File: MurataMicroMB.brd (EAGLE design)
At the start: 90 x 63 mm, 47 parts, among them CON1 C-2395.MurataMicroSD, CON3 CON_MIL_10_ARM, CON4 C-2395.microSD, IC1 74LVC1G00DBV, IC2 IC_DCDC_LM27313, IC3 IC_LPC11U3XQFN33, IC4 IC_LDO_XX1117_4, Q1 CLOCK_CRYSTAL_4_3225, SW1 SW_TACTSW_2PP8073, SW2 SW_TACTSW_2PP8073, SW3 SW_TACTSW_2PP8073, X1 TSW-102-02-S-S

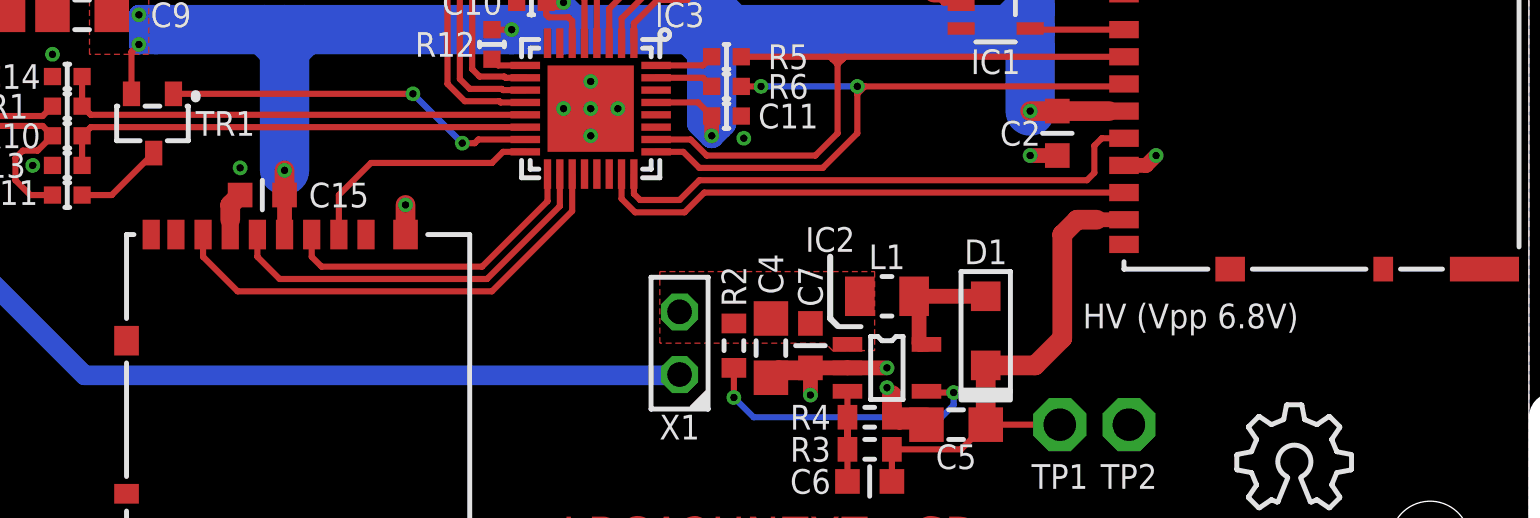
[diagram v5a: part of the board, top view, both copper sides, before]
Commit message: [ MB ] RCL value and size
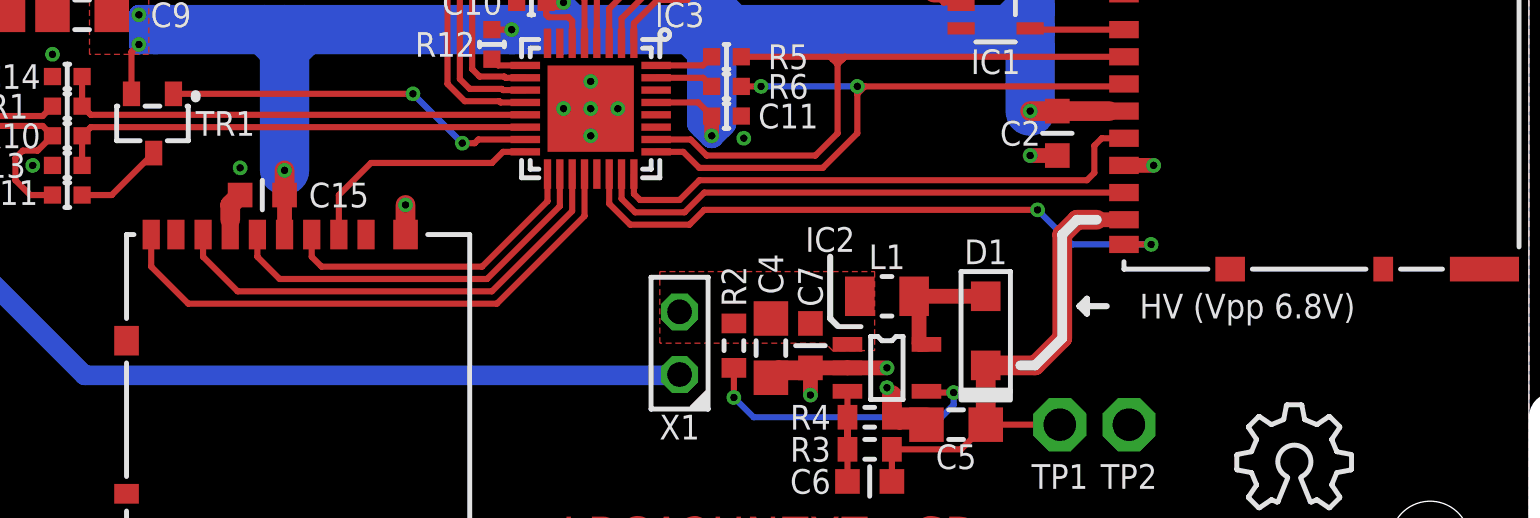
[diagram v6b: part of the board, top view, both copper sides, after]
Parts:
- C12, C3: value 18p -> 18p/1005
- C8, C9: value 4.7u -> 4.7u/1608
- R12, R7, R8, R9: value 10k -> 10k/1005
- R5, R6: value 100 -> 100/1005
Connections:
- new net DETECT1: CON1.SW_B, IC3.22
- new net DETECT2: CON4.SW_B, IC3.20
- net GND: now also CON1.SW_A, CON4.SW_A
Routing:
- net DETECT1: track 0.00 -> 25.4 mm, vias 0 -> 2
- net DETECT2: track 0.00 -> 22.6 mm
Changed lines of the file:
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@@
 <plain>
 <rectangle x1="53.6" y1="23.1" x2="54.4" y2="24.7" layer="41"/>
-<text x="66.3" y="23.1" size="1" layer="21" ratio="20" align="center">HV (Vpp 6.8V)</text>
+<text x="68.6" y="23.5" size="1" layer="21" ratio="20" align="center">HV (Vpp 6.8V)</text>
 <wire x1="59" y1="21.7" x2="59.7" y2="21.7" width="0.25" layer="41"/>
 <wire x1="59.7" y1="21.7" x2="60.5" y2="22.5" width="0.25" layer="41"/>
@@
 <wire x1="90.5" y1="53" x2="92.8" y2="53" width="0.25" layer="102"/>
 <text x="37.4" y="1.5" size="1.778" layer="21" ratio="17">board thickness t = 1.2mm</text>
+<wire x1="62.5" y1="27" x2="61.7" y2="27" width="0.4" layer="21"/>
+<wire x1="61.7" y1="27" x2="61.1" y2="26.4" width="0.4" layer="21"/>
+<wire x1="61.1" y1="26.4" x2="61.1" y2="22.2" width="0.4" layer="21"/>
+<wire x1="61.1" y1="22.2" x2="60" y2="21.1" width="0.4" layer="21"/>
+<wire x1="60" y1="21.1" x2="59.4" y2="21.1" width="0.4" layer="21"/>
+<wire x1="61.8" y1="23.5" x2="62.1" y2="23.8" width="0.25" layer="21"/>
+<wire x1="62.1" y1="23.8" x2="62.1" y2="23.2" width="0.25" layer="21"/>
+<wire x1="62.1" y1="23.2" x2="61.8" y2="23.5" width="0.25" layer="21"/>
+<wire x1="61.8" y1="23.5" x2="62.9" y2="23.5" width="0.25" layer="21"/>
 </plain>
 <attributes>
@@
 <attribute name="VALUE" x="37.4" y="34" size="1.27" layer="27" ratio="16" rot="R270"/>
 </element>
-<element name="C8" library="mylib" package="CR_2125" value="4.7u" x="17.2" y="35.3" smashed="yes">
+<element name="C8" library="mylib" package="CR_2125" value="4.7u/1608" x="17.2" y="35.3" smashed="yes">
 <attribute name="NAME" x="17.2" y="34" size="1" layer="25" ratio="20" align="center"/>
 <attribute name="VALUE" x="17.2" y="33.4" size="1" layer="27" ratio="20"/>
 </element>
-<element name="C9" library="mylib" package="CR_2125" value="4.7u" x="21.4" y="35.3" smashed="yes" rot="R180">
+<element name="C9" library="mylib" package="CR_2125" value="4.7u/1608" x="21.4" y="35.3" smashed="yes" rot="R180">
 <attribute name="NAME" x="25" y="35.3" size="1" layer="25" ratio="20" align="center"/>
 <attribute name="VALUE" x="21.4" y="37.2" size="1" layer="27" ratio="20" rot="R180"/>
@@
 <attribute name="VALUE" x="46.9" y="29.3" size="1" layer="27" font="vector" ratio="20"/>
 </element>
-<element name="R5" library="mylib" package="C0402" value="100" x="47.5" y="33.6" smashed="yes">
+<element name="R5" library="mylib" package="C0402" value="100/1005" x="47.5" y="33.6" smashed="yes">
 <attribute name="NAME" x="50" y="33.6" size="1" layer="25" font="vector" ratio="20" align="center"/>
 <attribute name="VALUE" x="46.9" y="31.7" size="1" layer="27" font="vector" ratio="20"/>
 </element>
-<element name="R6" library="mylib" package="C0402" value="100" x="47.5" y="32.4" smashed="yes">
+<element name="R6" library="mylib" package="C0402" value="100/1005" x="47.5" y="32.4" smashed="yes">
 <attribute name="NAME" x="50" y="32.4" size="1" layer="25" font="vector" ratio="20" align="center"/>
 <attribute name="VALUE" x="46.9" y="30.5" size="1" layer="27" font="vector" ratio="20"/>
 </element>
-<element name="R7" library="mylib" package="C0402" value="10k" x="46.9" y="38.9" smashed="yes" rot="R270">
+<element name="R7" library="mylib" package="C0402" value="10k/1005" x="46.9" y="38.9" smashed="yes" rot="R270">
 <attribute name="NAME" x="46.9" y="42" size="1" layer="25" font="vector" ratio="20" rot="R270" align="center"/>
 <attribute name="VALUE" x="45" y="39.5" size="1" layer="27" font="vector" ratio="20" rot="R270"/>
 </element>
-<element name="R8" library="mylib" package="C0402" value="10k" x="48.3" y="38.9" smashed="yes" rot="R270">
+<element name="R8" library="mylib" package="C0402" value="10k/1005" x="48.3" y="38.9" smashed="yes" rot="R270">
 <attribute name="NAME" x="48.3" y="42" size="1" layer="25" font="vector" ratio="20" rot="R270" align="center"/>
 <attribute name="VALUE" x="46.4" y="39.5" size="1" layer="27" font="vector" ratio="20" rot="R270"/>
 </element>
-<element name="R9" library="mylib" package="C0402" value="10k" x="45.5" y="38.9" smashed="yes" rot="R270">
+<element name="R9" library="mylib" package="C0402" value="10k/1005" x="45.5" y="38.9" smashed="yes" rot="R270">
 <attribute name="NAME" x="45.5" y="42" size="1" layer="25" font="vector" ratio="20" rot="R270" align="center"/>
 <attribute name="VALUE" x="43.6" y="39.5" size="1" layer="27" font="vector" ratio="20" rot="R270"/>
@@
 <attribute name="NAME" x="39.4" y="39.5" size="1" layer="25" font="vector" ratio="20" rot="R180" align="center"/>
 </element>
-<element name="C3" library="mylib" package="C0402" value="18p" x="41.9" y="42.3" smashed="yes">
+<element name="C3" library="mylib" package="C0402" value="18p/1005" x="41.9" y="42.3" smashed="yes">
 <attribute name="NAME" x="39.8" y="42.3" size="1" layer="25" font="vector" ratio="20" rot="R180" align="center"/>
 <attribute name="VALUE" x="41.3" y="40.4" size="1" layer="27" font="vector" ratio="20"/>
 </element>
-<element name="C12" library="mylib" package="C0402" value="18p" x="44.3" y="38.9" smashed="yes" rot="R90">
+<element name="C12" library="mylib" package="C0402" value="18p/1005" x="44.3" y="38.9" smashed="yes" rot="R90">
 <attribute name="NAME" x="44.3" y="42.1" size="1" layer="25" font="vector" ratio="20" rot="R90" align="center"/>
 <attribute name="VALUE" x="46.2" y="38.3" size="1" layer="27" font="vector" ratio="20" rot="R90"/>
@@
 <attribute name="VALUE" x="21.4" y="29.9" size="1" layer="27" font="vector" ratio="20" rot="R180"/>
 </element>
-<element name="R12" library="mylib" package="C0402" value="10k" x="38" y="34.1" smashed="yes" rot="R270">
+<element name="R12" library="mylib" package="C0402" value="10k/1005" x="38" y="34.1" smashed="yes" rot="R270">
 <attribute name="NAME" x="36.1" y="34.1" size="1" layer="25" font="vector" ratio="20" align="center"/>
 <attribute name="VALUE" x="36.1" y="34.7" size="1" layer="27" font="vector" ratio="20" rot="R270"/>
@@
 <contactref element="C2" pad="2"/>
 <via x="59.8" y="29.6" extent="1-16" drill="0.3"/>
-<via x="64.9" y="29.6" extent="1-16" drill="0.3"/>
+<via x="64.8" y="29.2" extent="1-16" drill="0.3"/>
 <contactref element="CON1" pad="SHLD@4"/>
 <contactref element="CON1" pad="SHLD"/>
@@
 <wire x1="50.9" y1="19.9" x2="50.9" y2="21" width="0.6" layer="1"/>
 <wire x1="59.8" y1="29.6" x2="60.9" y2="29.6" width="0.6" layer="1"/>
-<wire x1="64.9" y1="29.6" x2="64.5" y2="29.2" width="0.6" layer="1"/>
-<wire x1="64.5" y1="29.2" x2="63.6" y2="29.2" width="0.6" layer="1"/>
+<wire x1="64.8" y1="29.2" x2="63.6" y2="29.2" width="0.6" layer="1"/>
 <contactref element="TP2" pad="TP"/>
 <contactref element="C8" pad="2"/>
@@
 <wire x1="41" y1="38.3" x2="41.1" y2="38.3" width="0.6" layer="1"/>
 <wire x1="34.5" y1="27.6" x2="34.5" y2="26.4" width="0.8" layer="1"/>
+<contactref element="CON4" pad="SW_A"/>
+<contactref element="CON1" pad="SW_A"/>
 </signal>
 <signal name="D-">
@@
 <wire x1="31.8" y1="28" x2="31.8" y2="26.4" width="0.25" layer="1"/>
 </signal>
+<signal name="DETECT2">
+<contactref element="IC3" pad="20"/>
+<contactref element="CON4" pad="SW_B"/>
+<wire x1="24.2" y1="26.4" x2="24.2" y2="25.1" width="0.25" layer="1"/>
+<wire x1="24.2" y1="25.1" x2="25.7" y2="23.6" width="0.25" layer="1"/>
+<wire x1="25.7" y1="23.6" x2="38.2" y2="23.6" width="0.25" layer="1"/>
+<wire x1="38.2" y1="23.6" x2="41.75" y2="27.15" width="0.25" layer="1"/>
+<wire x1="41.75" y1="28.85" x2="41.75" y2="27.15" width="0.25" layer="1"/>
+</signal>
+<signal name="DETECT1">
+<contactref element="IC3" pad="22"/>
+<contactref element="CON1" pad="SW_B"/>
+<wire x1="63.6" y1="26" x2="64.7" y2="26" width="0.25" layer="1"/>
+<via x="64.7" y="26" extent="1-16" drill="0.3"/>
+<wire x1="64.7" y1="26" x2="61.5" y2="26" width="0.25" layer="16"/>
+<wire x1="61.5" y1="26" x2="60.1" y2="27.4" width="0.25" layer="16"/>
+<via x="60.1" y="27.4" extent="1-16" drill="0.3"/>
+<wire x1="60.1" y1="27.4" x2="46.6" y2="27.4" width="0.25" layer="1"/>
+<wire x1="46.6" y1="27.4" x2="46" y2="26.8" width="0.25" layer="1"/>
+<wire x1="46" y1="26.8" x2="43.6" y2="26.8" width="0.25" layer="1"/>
+<wire x1="43.6" y1="26.8" x2="42.75" y2="27.65" width="0.25" layer="1"/>
+<wire x1="42.75" y1="28.85" x2="42.75" y2="27.65" width="0.25" layer="1"/>
+</signal>
 </signals>

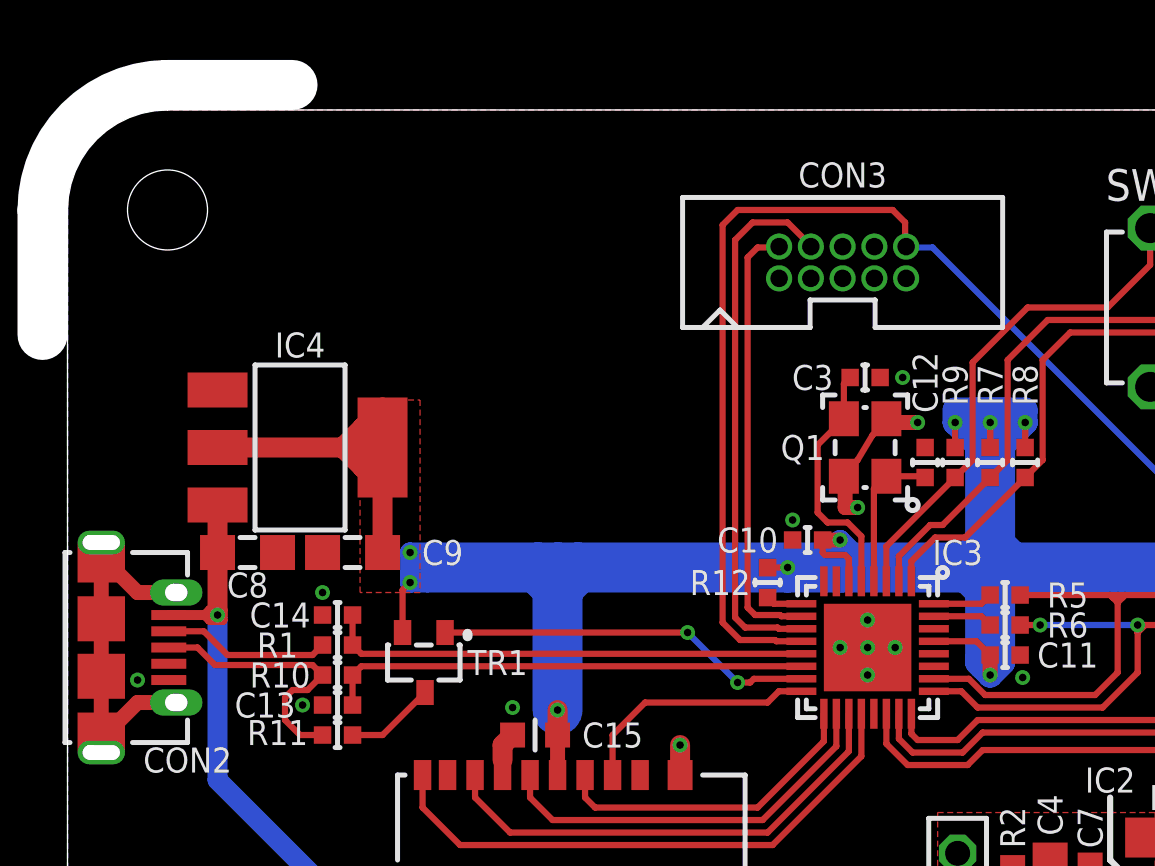
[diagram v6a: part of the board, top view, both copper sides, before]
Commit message: [ MB ] add LED1/R13/R14
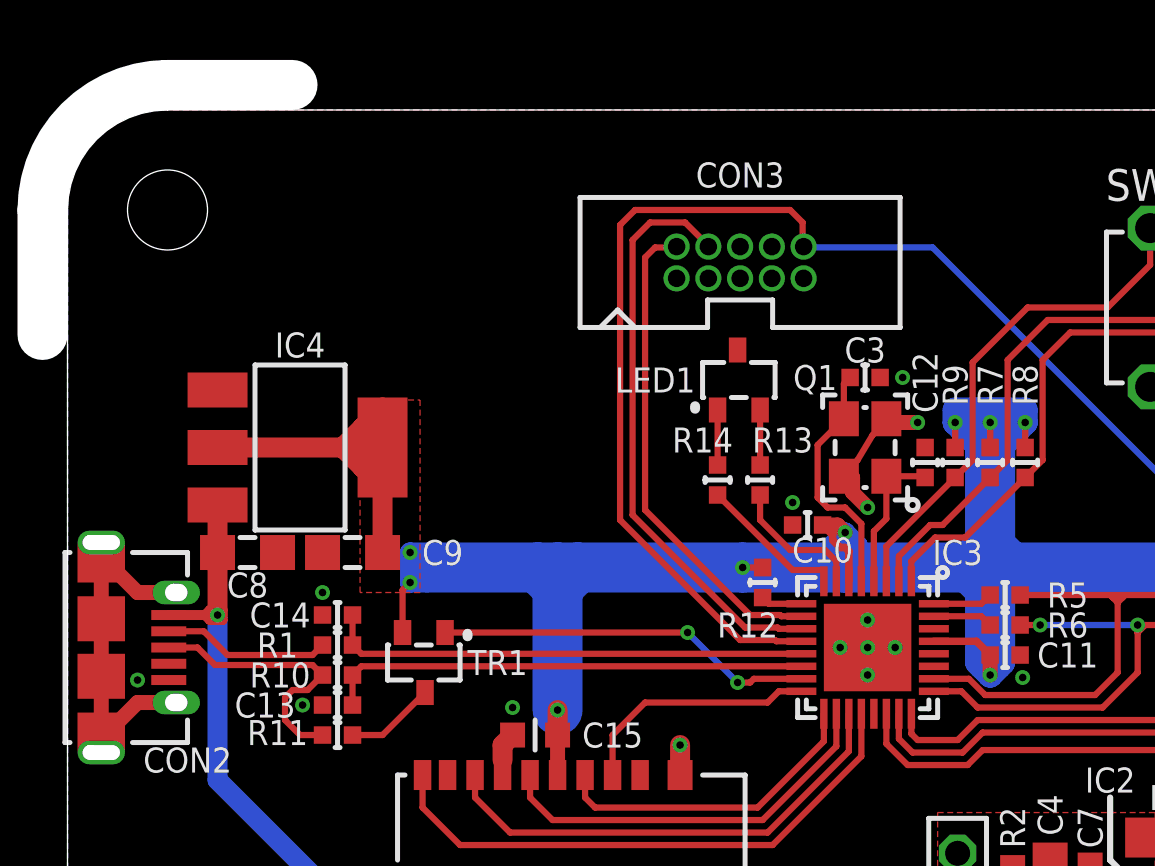
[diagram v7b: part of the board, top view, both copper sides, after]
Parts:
- added LED1: (no value), mylib:SOT95P300X140-3N
- added R13, R14: 100/1005, mylib:C0402
- IC2: value IC_DCDC_LM27313 -> 296-35164-1-ND
- moved CON3 4.10 mm to (36.9, 46.9)
- moved C10 0.60 mm to (39.6, 36.4)
- moved R12 0.20 mm to (37.8, 34.1)
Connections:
- new net N$1: IC3.8, R14.1
- new net N$14: IC3.7, R13.1
- new net N$15: LED1.2, R13.2
- new net N$16: LED1.1, R14.2
- net GND: now also LED1.3
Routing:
- net N$1: track 0.00 -> 5.94 mm
- net NSRST: track 48.7 -> 54.5 mm
- net N$14: track 0.00 -> 5.53 mm
- net N$16: track 0.00 -> 2.20 mm
- net N$15: track 0.00 -> 2.20 mm
- net SWDIO: track 17.7 -> 19.6 mm
- net SWCLK: track 21.7 -> 23.4 mm
- net 3.3V: track 134.7 -> 135.6 mm

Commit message: [ MB ][ SCH ] values and details change
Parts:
- C1, C10, C11: value 0.1u -> 0.1u/1005
- C15, C2, C7: value 0.1u -> 0.1u/1608
- C4, C5: value 4.7u -> 4.7u/2012
- C6: value NM -> NM/1608
- C8, C9: value 4.7u/1608 -> 4.7u/2012
- CON1: value C-2395.MurataMicroSD -> C-2395
- CON2: value (none) -> WM17143CT-ND
- CON4: value C-2395.microSD -> C-2395
- IC1: value 74LVC1G00DBV -> NC7SZ125M5XCT-ND
- IC4: value IC_LDO_XX1117_4 -> AZ1117EH-3.3TRG1DICT-ND
- LED1: value (none) -> 754-1633-1-ND
- Q1: value CLOCK_CRYSTAL_4_3225 -> 1253-1168-1-ND
- R2: value 10k -> 10k/1608
- R3: value 60.4k -> 60.4k/1608
- R4: value 13.3k -> 13.3k/1608
- SW1, SW2, SW3: value SW_TACTSW_2PP8073 -> P-8073
- moved PCB1 41.1 mm to (10.0, 10.0)
